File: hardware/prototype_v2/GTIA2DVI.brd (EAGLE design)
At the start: 70.2 x 53.3 mm, 25 parts, among them IC2 74AC541DW, IC4 GTIA, IC5 GTIA

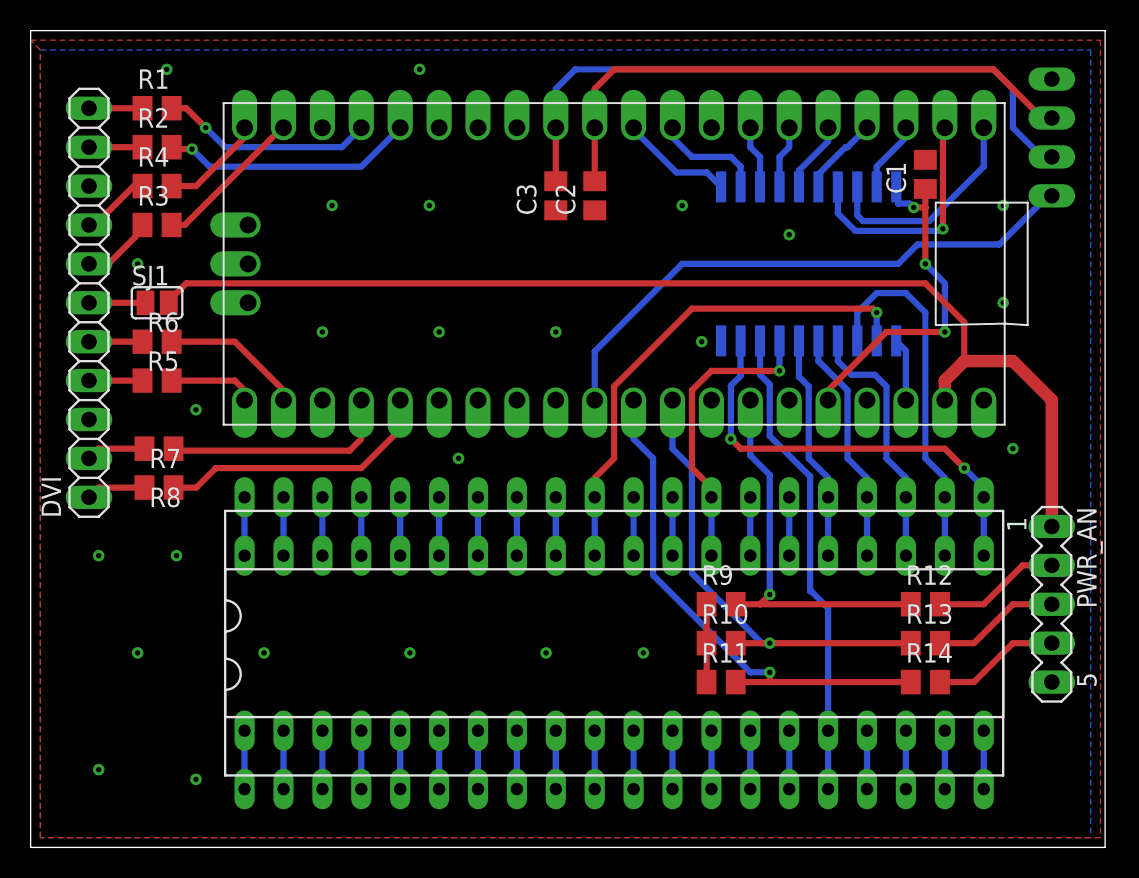
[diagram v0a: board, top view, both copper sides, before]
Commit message: moved to hardware UART buttons and UART pins changed
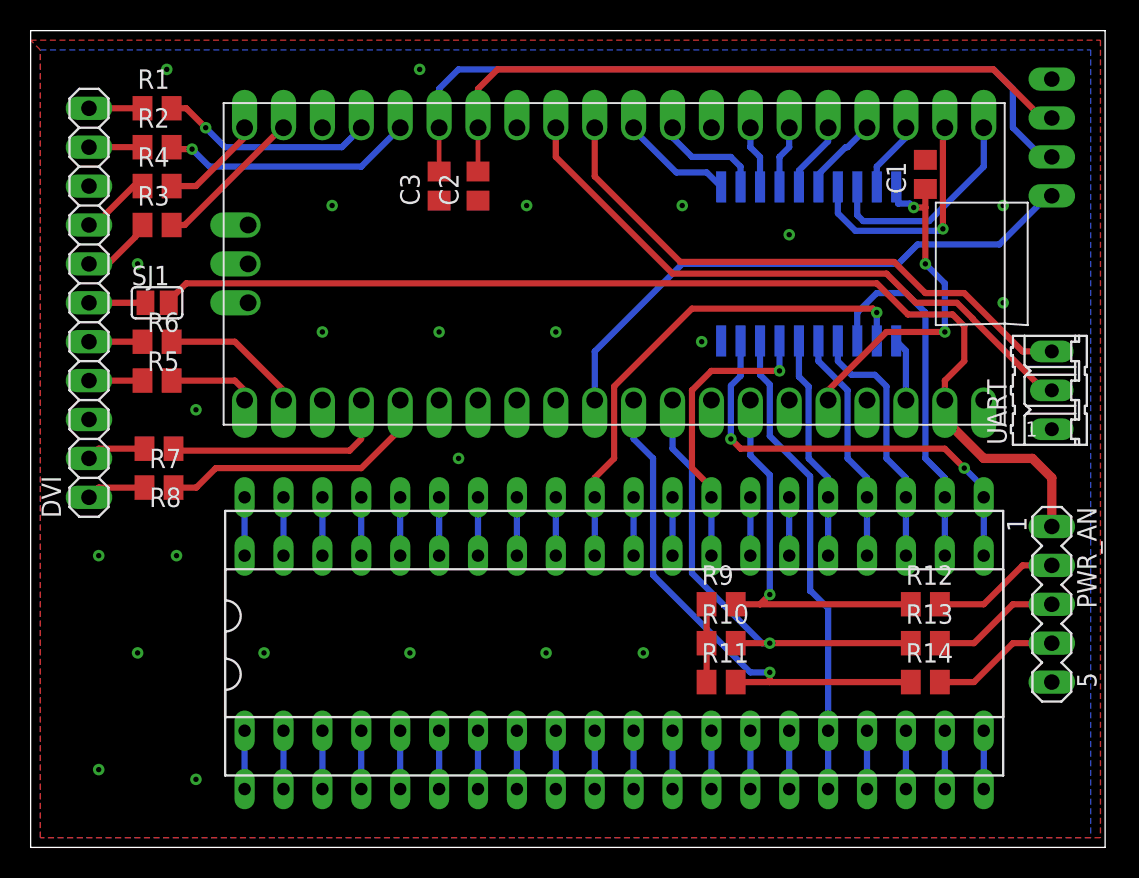
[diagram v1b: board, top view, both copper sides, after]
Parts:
- added UART: (no value), con-amp-quick:03P
- moved C2 7.65 mm to (29.2, 69.8)
- moved C3 7.65 mm to (26.7, 69.8)
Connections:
- new net UART_RX: UART.2, X1.GP9
- new net UART_TX: UART.3, X1.GP8
- net BTN_A: now also X1.GP10; no longer X1.GP8
- net BTN_B: now also X1.GP11; no longer X1.GP9
- net GND: now also UART.1
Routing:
- net UART_RX: track 0.00 -> 40.6 mm
- net UART_TX: track 0.00 -> 37.8 mm
- net BTN_A: track 37.7 -> 44.7 mm
- net BTN_B: track 42.8 -> 49.8 mm
- net VSYS_5V: track 78.0 -> 75.9 mm
